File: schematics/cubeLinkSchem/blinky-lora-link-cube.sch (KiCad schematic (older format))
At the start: 4 parts, among them J1 SMA Ant, U1 RPIHeader, U2 FEATHER_M0_BASIC_PROTO

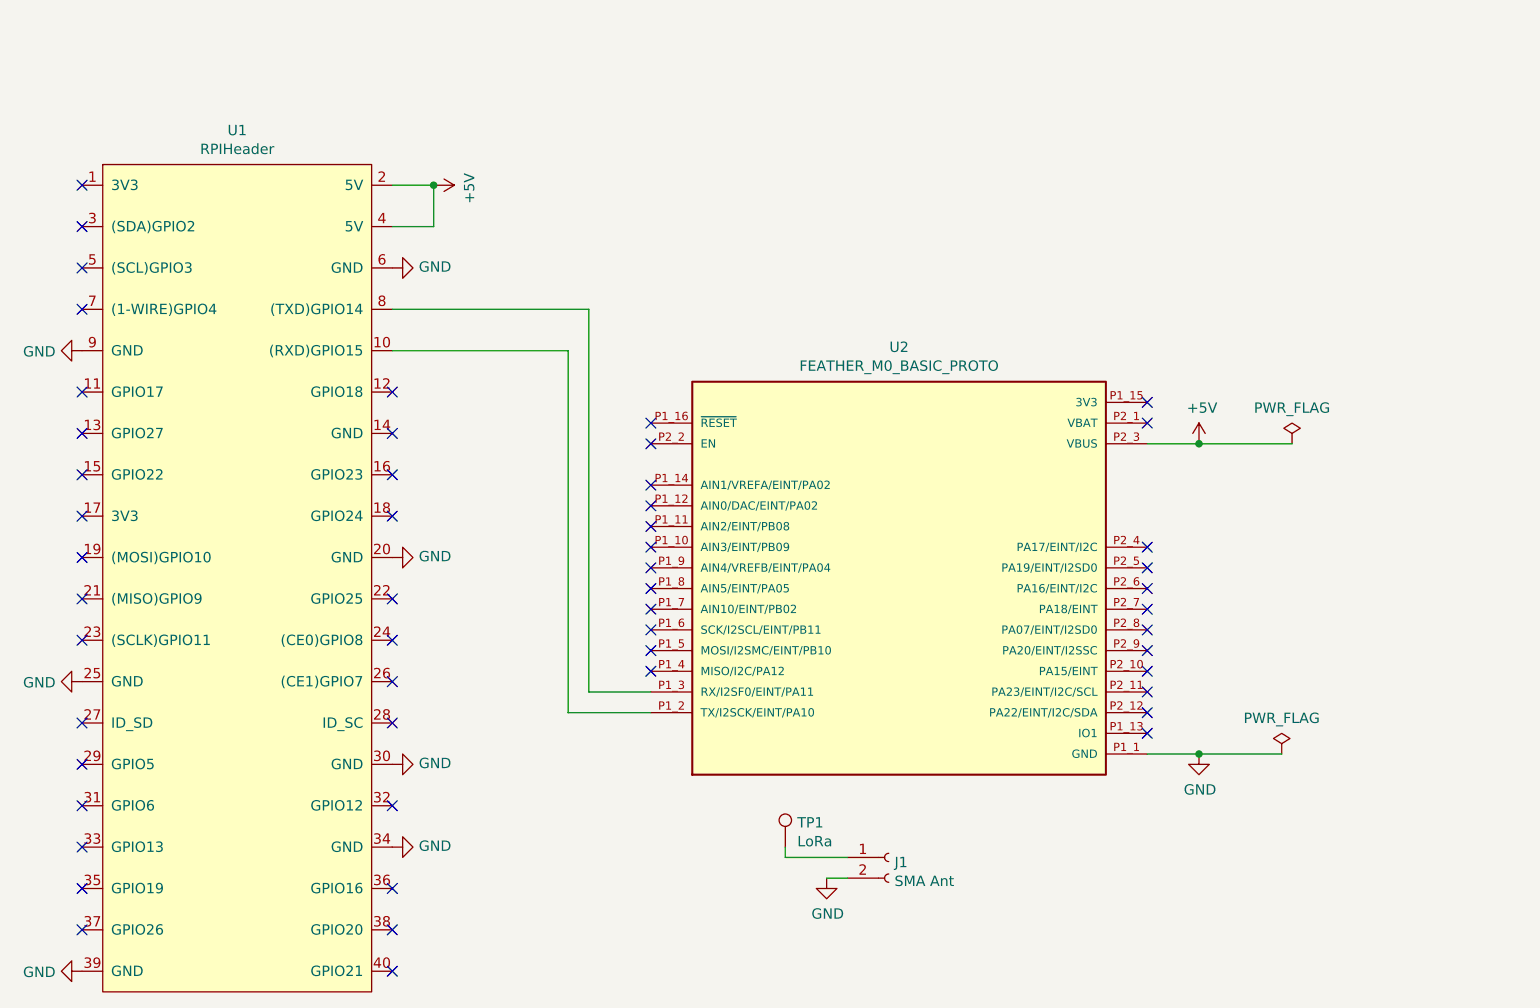
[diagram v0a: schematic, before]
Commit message: fixed lora footprint
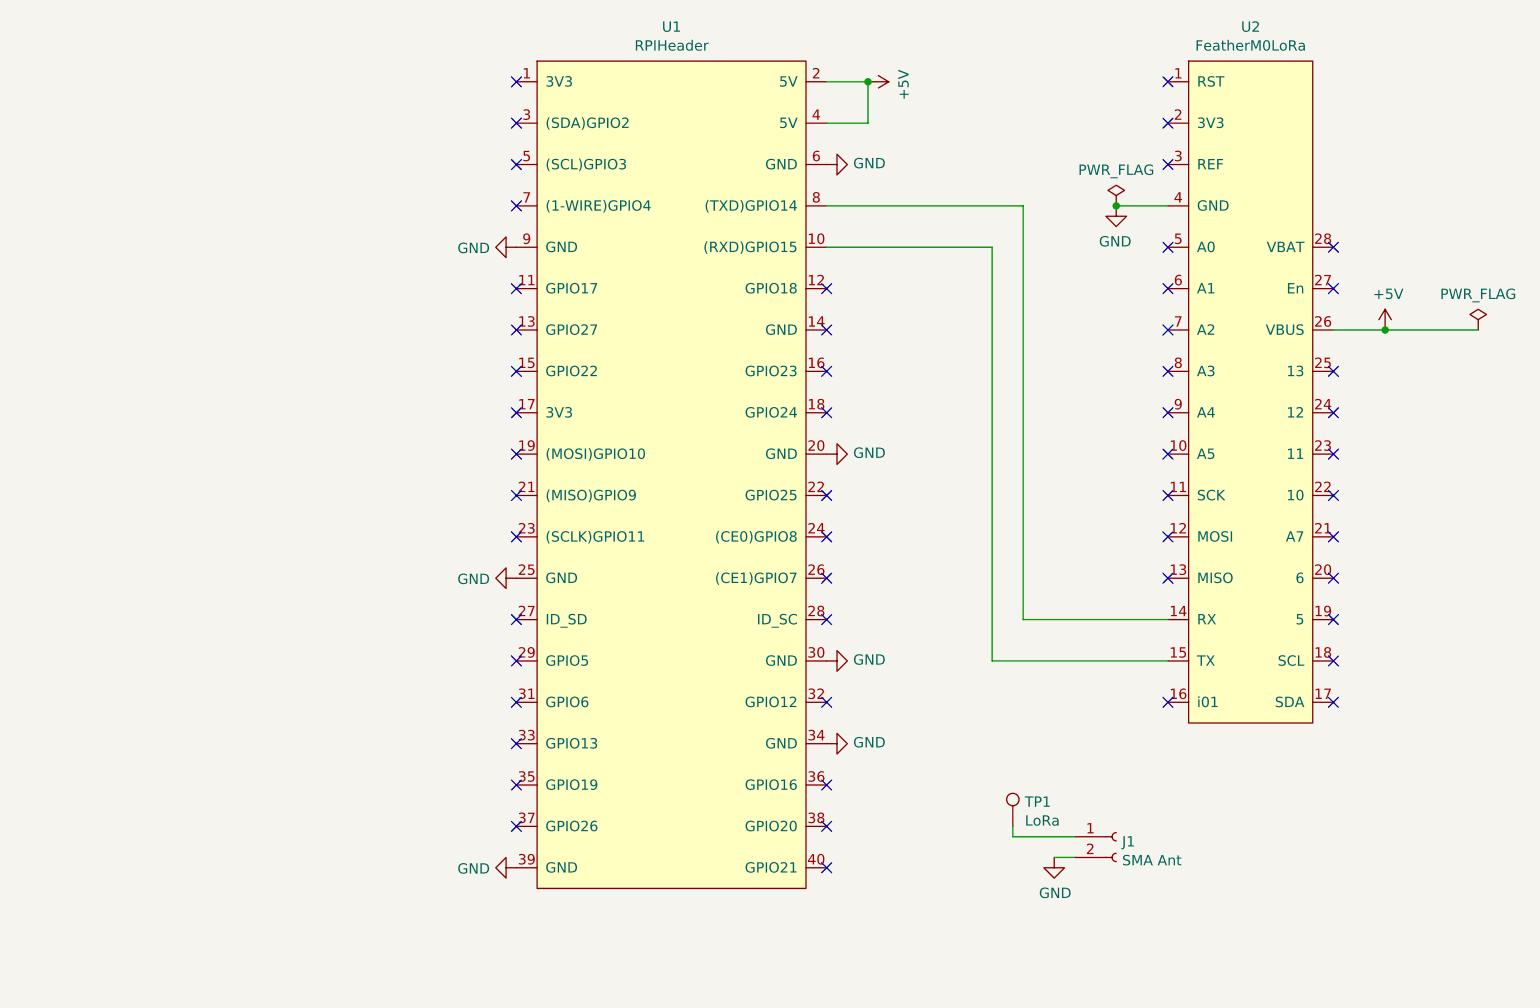
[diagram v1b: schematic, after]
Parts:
- removed U2: FEATHER_M0_BASIC_PROTO, FEATHER_M0_BASIC_PROTO:MODULE_FEATHER_M0_BASIC_PROTO, symbol FEATHER_M0_BASIC_PROTO:FEATHER_M0_BASIC_PROTO
- added U2: FeatherM0LoRa, dmcginnis427Footprints:FeatherM0LoRa, symbol dmcginnis427:FeatherM0LoRa
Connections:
- net +5V: now also U2.26 (VBUS)
- net GND: now also U2.4 (GND)
- net at U1.10 ((RXD)GPIO15): now also U2.15 (TX)
- net at U1.8 ((TXD)GPIO14): now also U2.14 (RX)
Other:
- moved on the sheet: J1, TP1, U1
